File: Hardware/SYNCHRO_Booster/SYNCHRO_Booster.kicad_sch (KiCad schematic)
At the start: 0 parts

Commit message: designing-backup
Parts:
- added C1: 100nF, symbol Device:C
- added C2, C3: 470uF, symbol Device:C_Polarized
- added C4: 10nF, symbol Device:C
- added C5, C6, C7: 22nF 50V, symbol Device:C
- added IC1: L6203, L6203:MULTIWATT-11, symbol SYNCHRO_Library:L6203
- added J1: Conn_01x02_Pin, symbol Connector:Conn_01x02_Pin
- added PS1: R-78E5.0-0.5, R-78E5.0-0.5:CONV_R-78E5.0-0.5, symbol SYNCHRO_Library:R-78E5.0-0.5
- added R1: 100m, Resistor_SMD:R_2512_6332Metric_Pad1.40x3.35mm_HandSolder, symbol SYNCHRO_Library:R_Sense
- added R2: 1k, symbol Device:R
- added R3: 15k, symbol Device:R
- added R4: 1k, symbol Device:R_Trim
- added R5: 4,7k, symbol Device:R
- added R6: 10, symbol Device:R
- added U1: LM393P, LM393P:DIP794W45P254L959H508Q8, symbol SYNCHRO_Library:LM393P
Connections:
- new net: C5.1, IC1.4 (CBOOT1)
- new net: C5.2, C7.1, IC1.3 (OUT1), J1.2 (Pin_2)
- new net: C4.2, IC1.9 (VREF)
- new net: C6.1, IC1.1 (OUT2), J1.1 (Pin_1), R6.2
- new net: IC1.10 (SENSE), R1.1, R2.2
- new net: IC1.11 (ENABLE), R5.2, U1.1 (1OUT)
- new net: C2.1, C3.1, IC1.2
- new net: C6.2, IC1.8 (CBOOT2)
- new net: C1.1, R2.1, U1.3 (1IN+)
- new net: C7.2, R6.1
- new net: R3.2, R4.1, U1.2 (1IN-)
- new net +5V: PS1.3 (+VOUT), R3.1, R5.1, U1.8 (VCC)
- new net GND1: C1.2, C2.2, C3.2, C4.1, IC1.6, PS1.2 (GND), R1.2, R4.2, U1.4 (GND)

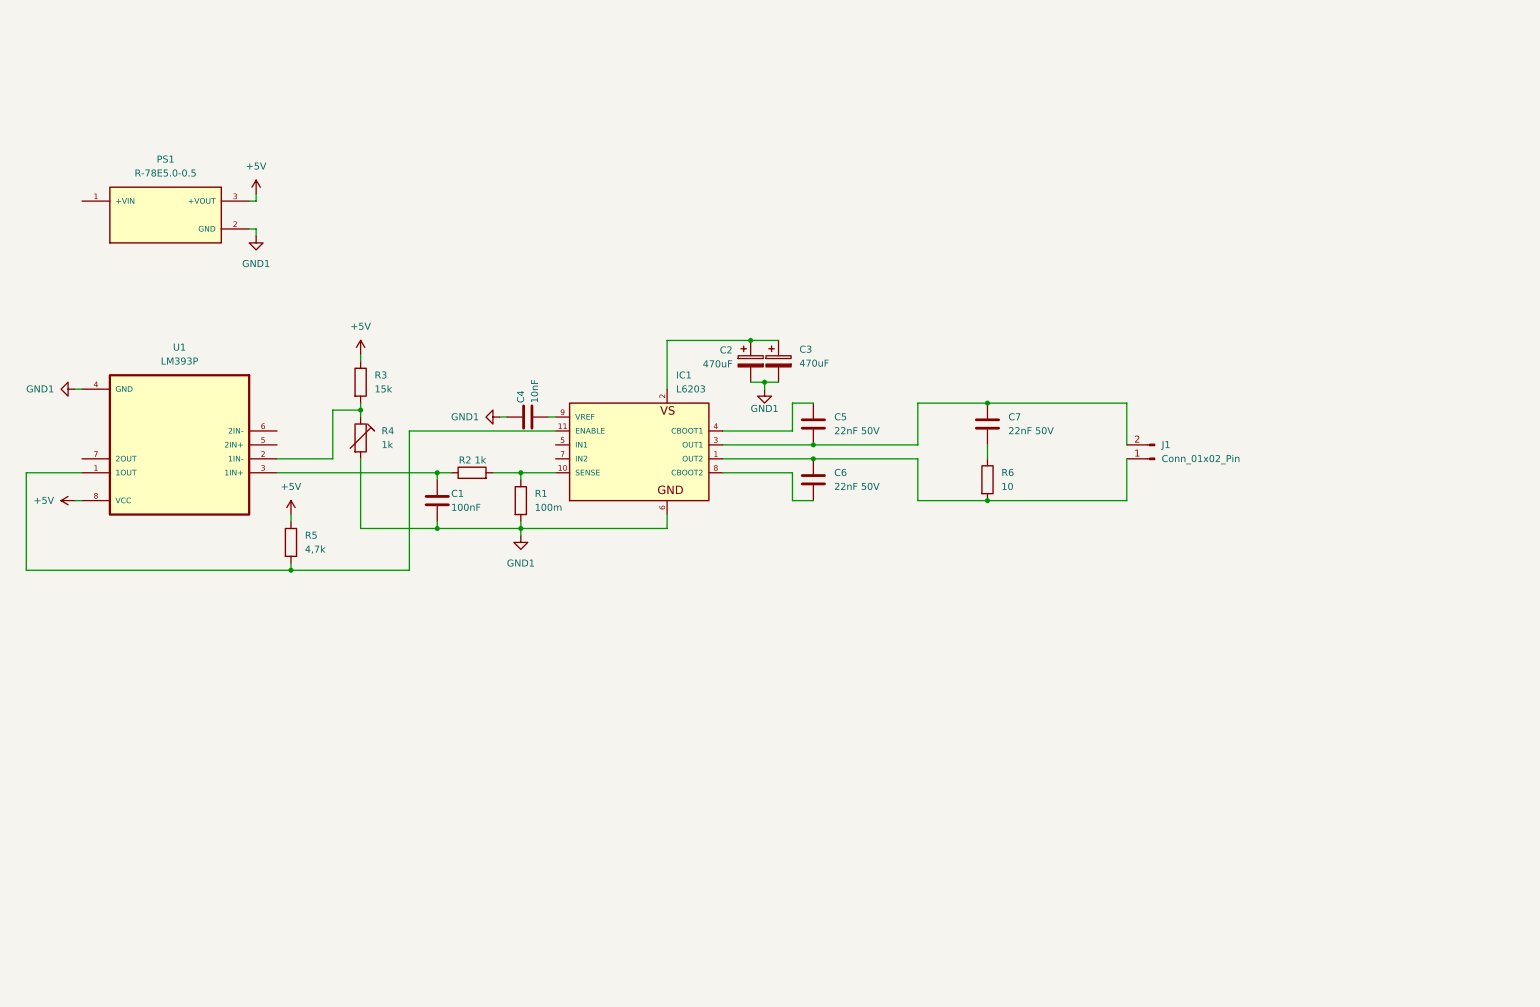
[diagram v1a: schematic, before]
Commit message: RJ45-Connection to booster
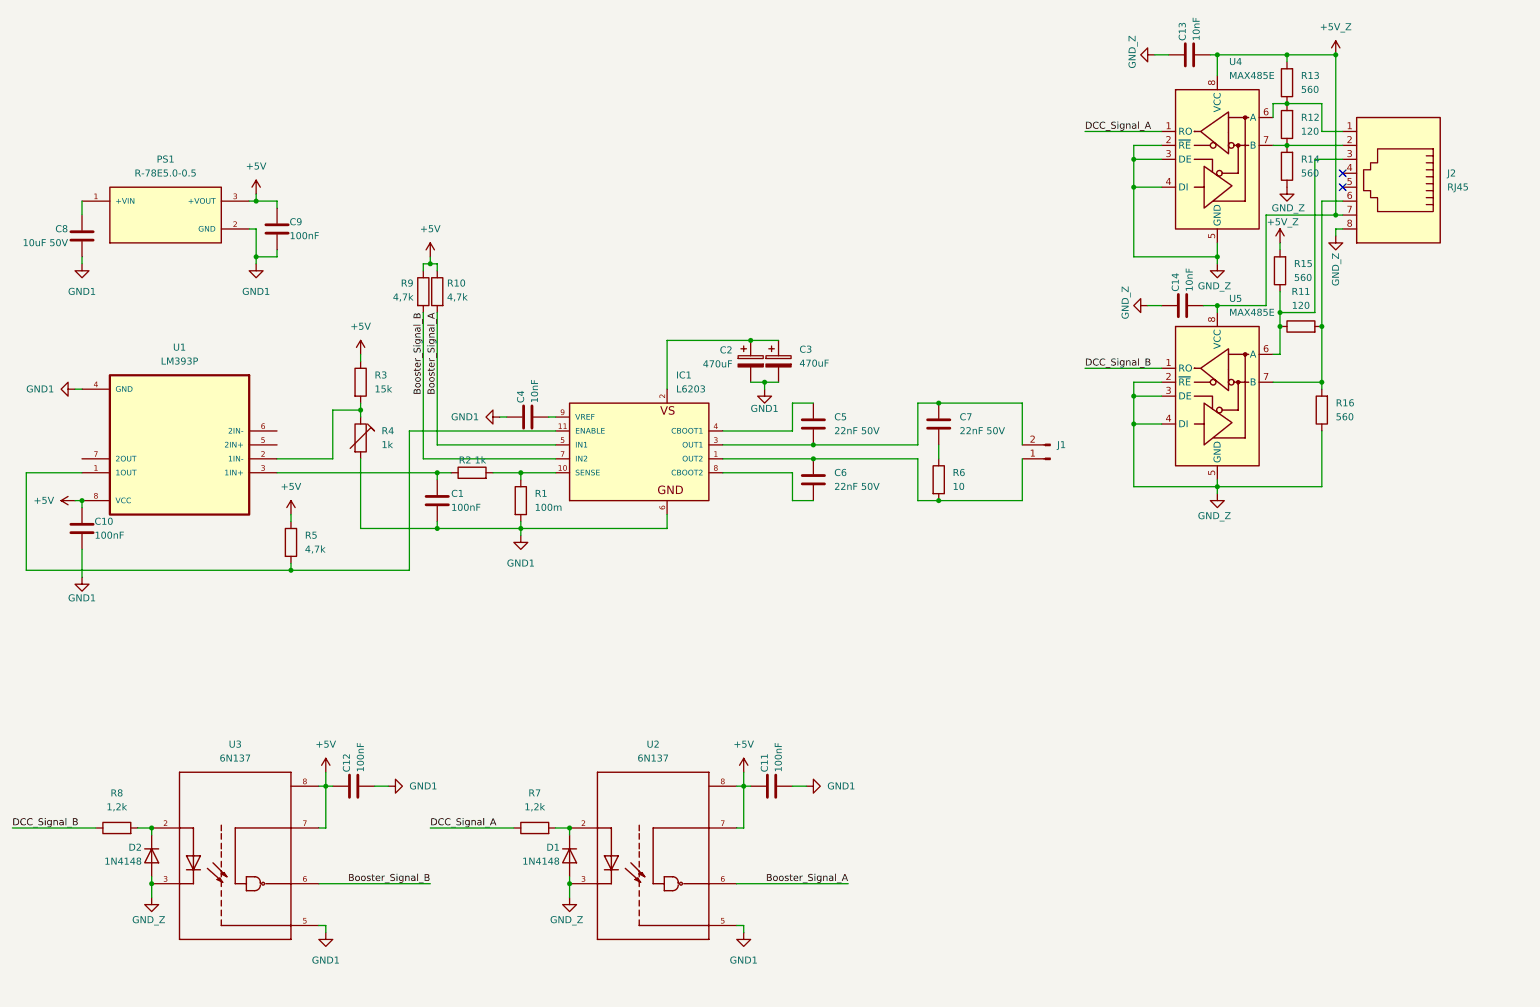
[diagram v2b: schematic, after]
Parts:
- added C10, C11, C12, C9: 100nF, symbol Device:C
- added C13, C14: 10nF, symbol Device:C
- added C8: 10uF 50V, symbol Device:C
- added D1, D2: 1N4148, Diode_THT:D_DO-35_SOD27_P7.62mm_Horizontal, symbol Diode:1N4148
- added J2: RJ45, symbol Connector:RJ45
- added R10, R9: 4,7k, symbol Device:R
- added R11, R12: 120, symbol Device:R
- added R13, R14, R15, R16: 560, symbol Device:R
- added R7, R8: 1,2k, symbol Device:R
- added U2, U3: 6N137, 6N137:DIP762W50P254L977H451Q8, symbol SYNCHRO_Library:6N137
- added U4, U5: MAX485E, Package_SO:SOIC-8_3.9x4.9mm_P1.27mm, symbol Interface_UART:MAX485E
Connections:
- net +5V: now also C10.1, C11.1, C12.1, C9.1, R10.1, R9.1, U2.7, U2.8, U3.7, U3.8
- net GND1: now also C10.2, C11.2, C12.2, C8.2, C9.2, U2.5, U3.5
- net at PS1.1 (+VIN): now also C8.1
- net Booster_Signal_A: now reaches IC1.5 (IN1)
- net Booster_Signal_A: now also R10.2, U2.6
- net Booster_Signal_B: now reaches IC1.7 (IN2)
- net Booster_Signal_B: now also R9.2, U3.6
- new net: D2.1 (K), R8.2, U3.2
- new net: J2.2, R12.1, R14.2, U4.7 (B)
- new net: J2.3, R11.1, R15.1, U5.6 (A)
- new net: J2.6, R11.2, R16.2, U5.7 (B)
- new net: D1.1 (K), R7.2, U2.2
- new net: J2.1, R12.2, R13.1, U4.6 (A)
- new net +5V_Z: C13.2, C14.2, J2.7, R13.2, R15.2, U4.8 (VCC), U5.8 (VCC)
- new net DCC_Signal_A: R7.1, U4.1 (RO)
- new net DCC_Signal_B: R8.1, U5.1 (RO)
- new net GND_Z: C13.1, C14.1, D1.2 (A), D2.2 (A), J2.8, R14.1, R16.1, U2.3, U3.3, U4.2 (~{RE}), U4.3 (DE), U4.4 (DI), U4.5 (GND), U5.2 (~{RE}), U5.3 (DE), U5.4 (DI), U5.5 (GND)
- no-connect marks 0 -> 2
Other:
- moved on the sheet: C7, J1, R6

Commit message: Booster Schematic Update
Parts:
- removed C13, C14: 10nF, symbol Device:C
- removed J2: RJ45, symbol Connector:RJ45
- removed R11, R12: 120, symbol Device:R
- removed R13, R14, R15, R16: 560, symbol Device:R
- removed U4, U5: MAX485E, Package_SO:SOIC-8_3.9x4.9mm_P1.27mm, symbol Interface_UART:MAX485E
- added J2: Power_Input, TerminalBlock_Phoenix:TerminalBlock_Phoenix_MKDS-1,5-2-5.08_1x02_P5.08mm_Horizontal, symbol Connector:Screw_Terminal_01x02
- added J3: B4B-XH-A, symbol SYNCHRO_Library:B4B-XH-A_LF__SN_
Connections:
- net +5V_Z: now also J3.1
- net DCC_Signal_A: now also J3.2
- net DCC_Signal_B: now also J3.3
- net GND1: now also J2.2 (Pin_2)
- net GND_Z: now also J3.4
- net +15V: now reaches C8.1, PS1.1 (+VIN)
- net +15V: now also C2.1, C3.1, IC1.2, J2.1 (Pin_1)
- net ENABLE: now reaches IC1.11 (ENABLE), R5.2, U1.1 (1OUT)
- net SENSE: now reaches C1.1, R2.1
- net SENSE: now also U1.2 (1IN-); no longer U1.3 (1IN+)
- net at R3.2, R4.1: now also U1.3 (1IN+); no longer U1.2 (1IN-)
- no-connect marks 2 -> 3
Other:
- note added: "https://is.gd/HZITAM"
- moved on the sheet: C1, C10, C11, C12, C2, C3, C4, C5, C6, C7, C8, C9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

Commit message: Updating design with RS-FlipFlop
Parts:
- removed R4: 1k, symbol Device:R_Trim
- added D3: SMAJ16CA-E3/61, Diode_SMD:D_SMA-SMB_Universal_Handsoldering, symbol Diode:SMAJ16CA
- added D4, D5: LED, LED_THT:LED_D5.0mm, symbol Device:LED
- added J4: Messpunkt, symbol Connector:Conn_01x02_Pin
- added R11: 10k, Resistor_SMD:R_0805_2012Metric_Pad1.20x1.40mm_HandSolder, symbol Device:R
- added R12, R13, R4: 1k, Resistor_SMD:R_0805_2012Metric_Pad1.20x1.40mm_HandSolder, symbol Device:R
- added SW1: SW_Push, Button_Switch_THT:SW_PUSH_6mm, symbol Switch:SW_Push
- added SW2: SW_SPDT, TerminalBlock_Phoenix:TerminalBlock_Phoenix_MKDS-3-3-5.08_1x03_P5.08mm_Horizontal, symbol Switch:SW_SPDT
- added U4: 74LVC2G02, Package_SO:VSSOP-8_2.3x2mm_P0.5mm, symbol 74xGxx:74LVC2G02
- C1, C10, C11, C12, C4, C9: footprint (none) -> Capacitor_THT:C_Disc_D5.0mm_W2.5mm_P5.00mm
- C2, C3: footprint (none) -> Capacitor_THT:CP_Radial_D10.0mm_P5.00mm
- C5, C6, C7, C8: footprint (none) -> Capacitor_THT:C_Rect_L7.0mm_W2.5mm_P5.00mm
- IC1: footprint L6203:MULTIWATT-11 -> SYNCHRO_Library:MULTIWATT-11
- J1: footprint (none) -> TerminalBlock_Phoenix:TerminalBlock_Phoenix_MKDS-1,5-2-5.08_1x02_P5.08mm_Horizontal
- J3: footprint (none) -> SYNCHRO_Library:JST_B4B-XH-A_LF__SN_
- PS1: footprint R-78E5.0-0.5:CONV_R-78E5.0-0.5 -> SYNCHRO_Library:CONV_R-78E5.0-0.5
- R10, R2, R5, R6, R7, R8, R9: footprint (none) -> Resistor_SMD:R_0805_2012Metric_Pad1.20x1.40mm_HandSolder
- R3: value 15k -> 24k; footprint (none) -> Resistor_SMD:R_0805_2012Metric_Pad1.20x1.40mm_HandSolder
- U1: footprint LM393P:DIP794W45P254L959H508Q8 -> SYNCHRO_Library:DIP762W50P254L977H451Q8
- U2, U3: footprint 6N137:DIP762W50P254L977H451Q8 -> SYNCHRO_Library:DIP762W50P254L977H451Q8
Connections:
- net +15V: now also SW2.1 (A); no longer J2.1 (Pin_1)
- net +5V: now also U1.6 (2IN-), J4.1 (Pin_1), R12.1, R13.1, SW1.1, U4.8 (VCC)
- net ENABLE: now also D5.1 (K), U4.5, U4.7; no longer R5.2, U1.1 (1OUT)
- net GND1: now also U1.5 (2IN+), D4.1 (K), J4.2 (Pin_2), R11.2, R4.2, U4.4 (GND)
- net SENSE: now also U1.3 (1IN+); no longer U1.2 (1IN-)
- net at C5.2, C7.1, IC1.3 (OUT1)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: now also D3.1 (A1)
- net at C6.1, IC1.1 (OUT2), J1.1 (Pin_1)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: now also D3.2 (A2)
- net at R3.2: now also U1.2 (1IN-), R4.1; no longer U1.3 (1IN+)
- new net: R11.1, SW1.2, U4.6
- new net: J2.1 (Pin_1), SW2.2 (B), SW2.3 (C)
- new net: R5.2, U1.1 (1OUT), U4.1
- new net: U4.2, U4.3
- new net: D4.2 (A), R12.2
- new net: D5.2 (A), R13.2
- no-connect marks 3 -> 1
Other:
- note added: "SN74LVC2G02DCUR"
- note removed: "https://is.gd/HZITAM"
- moved on the sheet: C1, C12, C2, C3, C4, C5, C6, C7, C8, C9, D2, IC1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
